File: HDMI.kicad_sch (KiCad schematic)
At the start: 8 parts, among them IC6 TPS2553QDBVRQ1, J9 HDMI_E

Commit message: small changes for ravi
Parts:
- removed C44: 100n, Capacitor_SMD:C_0402_1005Metric, symbol Device:C
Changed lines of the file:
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@@
-	)
-	(junction
-		(at 201.93 133.35)
-		(diameter 0)
-		(color 0 0 0 0)
 	)
 	(junction
@@
 	(wire
 		(pts
-			(xy 201.93 133.35) (xy 212.09 133.35)
-		)
-		(stroke
-			(width 0)
-			(type default)
-		)
-	)
-	(wire
-		(pts
 			(xy 146.05 120.65) (xy 152.4 120.65)
 		)
@@
 	(wire
 		(pts
-			(xy 185.42 133.35) (xy 201.93 133.35)
+			(xy 185.42 133.35) (xy 212.09 133.35)
 		)
 		(stroke
@@
 	(wire
 		(pts
-			(xy 201.93 146.05) (xy 201.93 149.86)
-		)
-		(stroke
-			(width 0)
-			(type default)
-		)
-	)
-	(wire
-		(pts
 			(xy 109.22 107.95) (xy 111.76 107.95)
 		)
@@
 		(pts
 			(xy 149.86 138.43) (xy 157.48 138.43)
-		)
-		(stroke
-			(width 0)
-			(type default)
-		)
-	)
-	(wire
-		(pts
-			(xy 201.93 133.35) (xy 201.93 138.43)
 		)
 		(stroke
@@
 			)
 		)
-		(property "Datasheet" ""
+		(property "Datasheet" "https://datasheets.raspberrypi.com/cm4/cm4-datasheet.pdf"
 			(at 81.28 127 0)
 			(effects
@@
 					(unit 1)
 				)
-			)
-		)
-	)
-	(symbol
-		(lib_id "Device:C")
-		(at 201.93 142.24 0)
-		(unit 1)
-		(exclude_from_sim no)
-		(in_bom yes)
-		(on_board yes)
-		(dnp no)
-		(property "Reference" "C44"
-			(at 204.851 141.0716 0)
-			(effects
-				(font
-					(size 1.27 1.27)
-				)
-				(justify left)
-			)
-		)
-		(property "Value" "100n"
-			(at 204.851 143.383 0)
-			(effects
-				(font
-					(size 1.27 1.27)
-				)
-				(justify left)
-			)
-		)
-		(property "Footprint" "Capacitor_SMD:C_0402_1005Metric"
-			(at 202.8952 146.05 0)
-			(effects
-				(font
-					(size 1.27 1.27)
-				)
-				(hide yes)
-			)
-		)
-		(property "Datasheet" "https://search.murata.co.jp/Ceramy/image/img/A01X/G101/ENG/GRM155R71C104KA88-01.pdf"
-			(at 201.93 142.24 0)
-			(effects
-				(font
-					(size 1.27 1.27)
-				)
-				(hide yes)
-			)
-		)
-		(property "Description" ""
-			(at 201.93 142.24 0)
-			(effects
-				(font
-					(size 1.27 1.27)
-				)
-				(hide yes)
-			)
-		)
-		(property "Field4" "Farnell"
-			(at 201.93 142.24 0)
-			(effects
-				(font
-					(size 1.27 1.27)
-				)
-				(hide yes)
-			)
-		)
-		(property "Field5" "2611911"
-			(at 201.93 142.24 0)
-			(effects
-				(font
-					(size 1.27 1.27)
-				)
-				(hide yes)
-			)
-		)
-		(property "Field6" "RM EMK105 B7104KV-F"
-			(at 201.93 142.24 0)
-			(effects
-				(font
-					(size 1.27 1.27)
-				)
-				(hide yes)
-			)
-		)
-		(property "Field7" "TAIYO YUDEN EUROPE GMBH"
-			(at 201.93 142.24 0)
-			(effects
-				(font
-					(size 1.27 1.27)
-				)
-				(hide yes)
-			)
-		)
-		(property "Part Description" "	0.1uF 10% 16V Ceramic Capacitor X7R 0402 (1005 Metric)"
-			(at 201.93 142.24 0)
-			(effects
-				(font
-					(size 1.27 1.27)
-				)
-				(hide yes)
-			)
-		)
-		(property "Field8" "110091611"
-			(at 201.93 142.24 0)
-			(effects
-				(font
-					(size 1.27 1.27)
-				)
-				(hide yes)
-			)
-		)
-		(pin "1"
-		)
-		(pin "2"
-		)
-		(instances
-			(project "PiBoard"
-				(path "/e4d65698-b8ec-4bf6-9f2b-a5010377155a/2dec5fd6-8756-425d-9ae9-2f1c2fc4e6c1"
-					(reference "C44")
-					(unit 1)
-				)
-			)
-		)
-	)
-	(symbol
-		(lib_name "GND_1")
-		(lib_id "power:GND")
-		(at 201.93 149.86 0)
-		(unit 1)
-		(exclude_from_sim no)
-		(in_bom yes)
-		(on_board yes)
-		(dnp no)
-		(fields_autoplaced yes)
-		(property "Reference" "#PWR063"
-			(at 201.93 156.21 0)
-			(effects
-				(font
-					(size 1.27 1.27)
-				)
-				(hide yes)
-			)
-		)
-		(property "Value" "GND"
-			(at 201.93 154.94 0)
-			(effects
-				(font
-					(size 1.27 1.27)
-				)
-				(hide yes)
-			)
-		)
-		(property "Footprint" ""
-			(at 201.93 149.86 0)
-			(effects
-				(font
-					(size 1.27 1.27)
-				)
-				(hide yes)
-			)
-		)
-		(property "Datasheet" ""
-			(at 201.93 149.86 0)
-			(effects
-				(font
-					(size 1.27 1.27)
-				)
-				(hide yes)
-			)
-		)
-		(property "Description" "Power symbol creates a global label with name \"GND\" , ground"
-			(at 201.93 149.86 0)
-			(effects
-				(font
-					(size 1.27 1.27)
-				)
-				(hide yes)
-			)
-		)
-		(pin "1"
-		)
-		(instances
-			(project "PiBoard"
-				(path "/e4d65698-b8ec-4bf6-9f2b-a5010377155a/2dec5fd6-8756-425d-9ae9-2f1c2fc4e6c1"
-					(reference "#PWR063")
-					(unit 1)
-				)

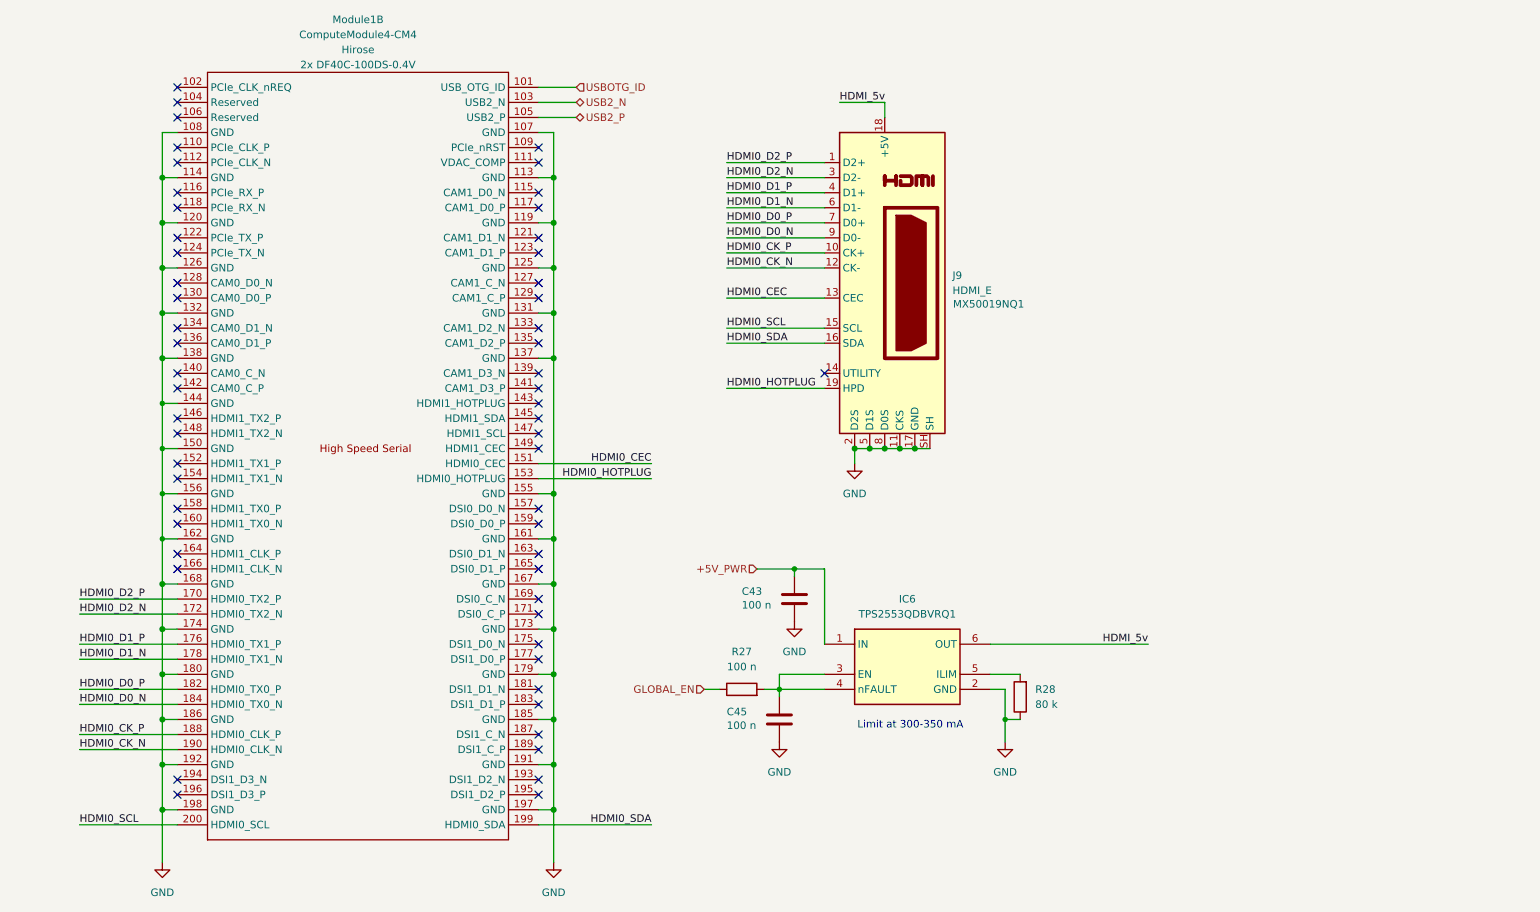
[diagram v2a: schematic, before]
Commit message: added parts to almost everything (except can xtal and fuses)
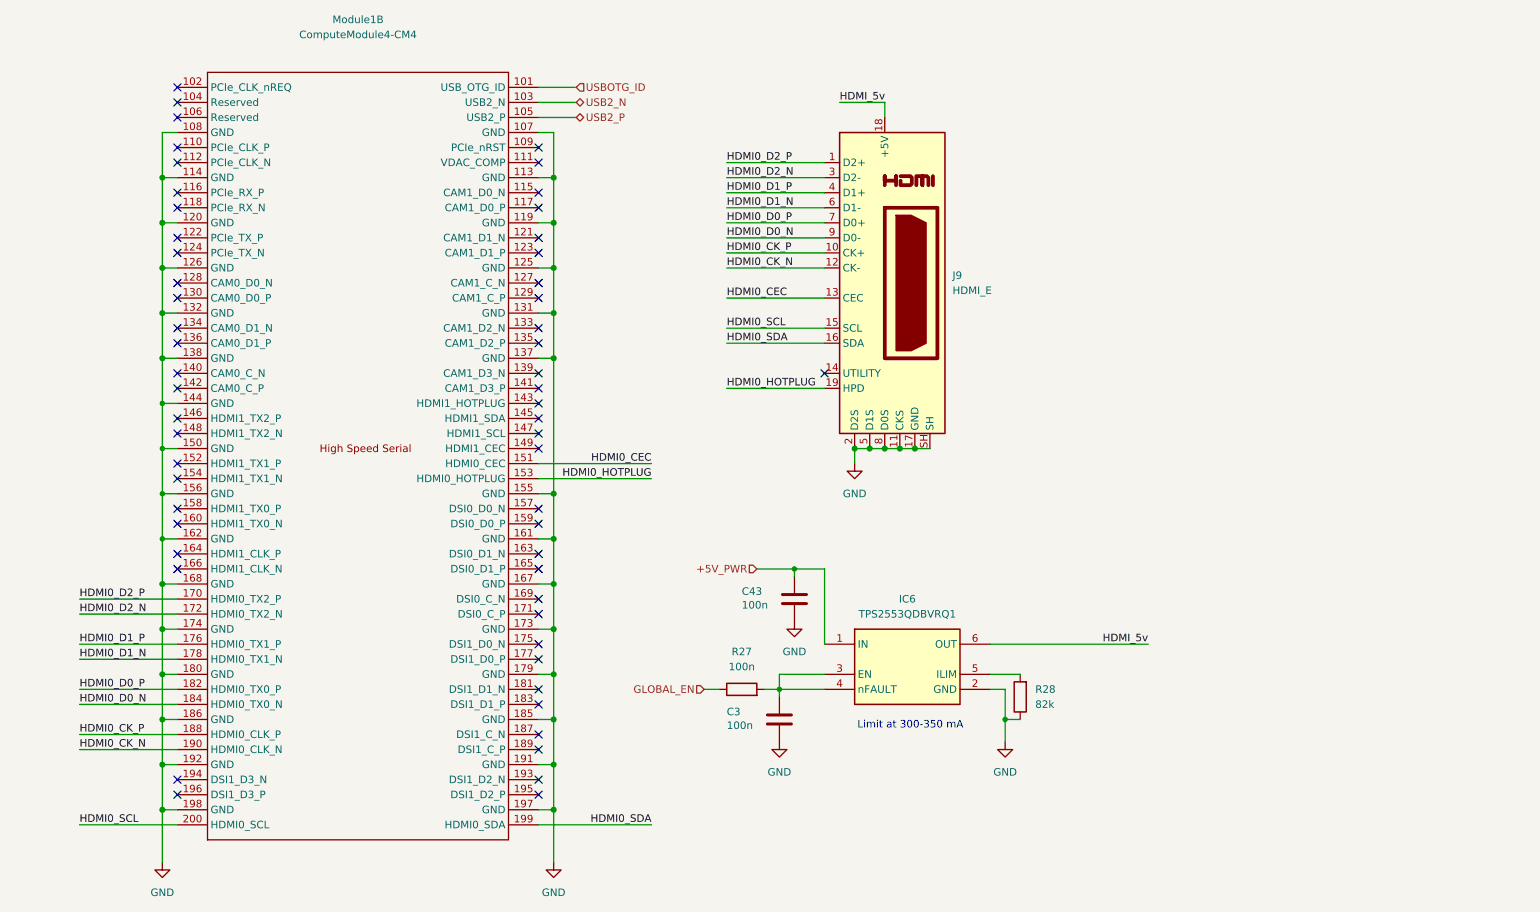
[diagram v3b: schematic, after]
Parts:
- removed C45: 100 n, Capacitor_SMD:C_0402_1005Metric, symbol Device:C
- added C3: 100n, Capacitor_SMD:C_0805_2012Metric, symbol Device:C
- C43: value 100 n -> 100n; footprint Capacitor_SMD:C_0402_1005Metric -> Capacitor_SMD:C_0805_2012Metric; Field4 Farnell -> (none); Field5 2611911 -> (none); Field6 RM EMK105 B7104KV-F -> (none); Field7 TAIYO YUDEN EUROPE GMBH -> (none); Field8 110091611 -> (none); P/N (none) -> C0805C104M5RACTU; Part Description 0.1uF 10% 16V Ceramic Capacitor X7R 0402 (1005 Metric) -> (none)
- IC6: footprint SOT95P280X145-6N -> Controls_Pi:SOT95P280X145-6N; Arrow Part Number TPS2553QDBVRQ1 -> (none); Arrow Price/Stock https://www.arrow.com/en/products/tps2553qdbvrq1/texas-inst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 -> (none); Height 1.45 -> (none); Manufacturer_Name Texas Instruments -> (none); Manufacturer_Part_Number TPS2553QDBVRQ1 -> (none); Mouser Part Number 595-TPS2553QDBVRQ1 -> (none); Mouser Price/Stock https://www.mouser.co.uk/ProductDetail/Texas-Instruments/TP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 -> (none); P/N (none) -> TPS2553QDBVRQ1
- J9: footprint (none) -> Controls_Pi:MX50019NQ1; Part No MX50019NQ1 -> (none)
- Module1: Field4 Hirose -> (none); Field5 2x DF40C-100DS-0.4V -> (none)
- R27: value 100 n -> 100n; footprint (none) -> Resistor_SMD:R_0805_2012Metric; P/N (none) -> CRCW0805100KFKEAC
- R28: value 80 k -> 82k; footprint (none) -> Resistor_SMD:R_1210_3225Metric; P/N (none) -> CRMA1210AF82K0FKEF
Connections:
- net GND: now also C3.2
- net at IC6.3 (EN), IC6.4 (nFAULT), R27.2: now also C3.1

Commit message: fixed cap sizes, added remaining parts, fixed rtc battery
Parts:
- J9: P/N (none) -> MX50019NQ1
- Module1: P/N (none) -> DF40C-100DS-0.4V
- R28: footprint Resistor_SMD:R_1210_3225Metric -> Resistor_SMD:R_0805_2012Metric; P/N CRMA1210AF82K0FKEF -> CRCW080582K0FKEAC
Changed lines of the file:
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@@
+			)
+		)
+		(property "P/N" "MX50019NQ1"
+			(at 167.64 72.39 0)
+			(effects
+				(font
+					(size 1.27 1.27)
+				)
+				(hide yes)
 			)
 		)
@@
 			)
 		)
-		(property "Footprint" "Resistor_SMD:R_1210_3225Metric"
+		(property "Footprint" "Resistor_SMD:R_0805_2012Metric"
 			(at 192.278 142.24 90)
 			(effects
@@
 			)
 		)
-		(property "Datasheet" "https://www.vishay.com/docs/68043/crma.pdf"
+		(property "Datasheet" "https://www.vishay.com/docs/28773/crcwce3.pdf"
 			(at 190.5 142.24 0)
 			(effects
@@
 			)
 		)
-		(property "Description" "Resistor 82k, 1%, 100PPM"
+		(property "Description" "Resistor 82k 1% 125mW"
 			(at 190.5 142.24 0)
 			(effects
@@
 			)
 		)
-		(property "P/N" "CRMA1210AF82K0FKEF"
+		(property "P/N" "CRCW080582K0FKEAC"
 			(at 190.5 142.24 0)
 			(effects
@@
 			)
 		)
-		(property "Description" ""
+		(property "Description" "100 Position Connector Receptacle, Center Strip Contacts Surface Mount Gold"
 			(at -60.96 100.33 0)
 			(effects
+				(font
+					(size 1.27 1.27)
+				)
+				(hide yes)
+			)
+		)
+		(property "P/N" "DF40C-100DS-0.4V"
+			(at -60.96 100.33 0)
+			(effects

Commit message: review committee changes implmented
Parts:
- added D10, D8: ESD204DQAR, Controls_Pi:ESD204DQAR, symbol ESD204DQAR:ESD204DQAR
- added D12: TPD4E05U06DQAR, DQA(R-PUSON-N10), symbol TPD4E05U06DQAR:TPD4E05U06DQAR
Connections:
- net GND: now also D10.3 (GND_1), D10.8 (GND_2), D8.3 (GND_1), D8.8 (GND_2)
- net HDMI0_CEC: now also D12.4 (D2+); no longer J9.13 (CEC)
- net HDMI0_CK_N: now also D10.5 (IO4); no longer J9.12 (CK-)
- net HDMI0_CK_P: now also D10.4 (IO3); no longer J9.10 (CK+)
- net HDMI0_D0_N: now also D8.2 (IO2); no longer J9.9 (D0-)
- net HDMI0_D0_P: now also D8.1 (IO1); no longer J9.7 (D0+)
- net HDMI0_D1_N: now also D8.5 (IO4); no longer J9.6 (D1-)
- net HDMI0_D1_P: now also D8.4 (IO3); no longer J9.4 (D1+)
- net HDMI0_D2_N: now also D10.2 (IO2); no longer J9.3 (D2-)
- net HDMI0_D2_P: now also D10.1 (IO1); no longer J9.1 (D2+)
- net HDMI0_SCL: now also D12.1 (D1+); no longer J9.15 (SCL)
- net HDMI0_SDA: now also D12.2 (D1-); no longer J9.16 (SDA)
- net HDMI_5v renamed HDMI_5V
- new net HDMI0_CEC_P: D12.7 (NC_2), J9.13 (CEC)
- new net HDMI0_CK_N_P: D10.7 (NC_2), J9.12 (CK-)
- new net HDMI0_CK_P_P: D10.6 (NC_1), J9.10 (CK+)
- new net HDMI0_D0_N_P: D8.10 (NC_4), J9.9 (D0-)
- new net HDMI0_D0_P_P: D8.9 (NC_3), J9.7 (D0+)
- new net HDMI0_D1_N_P: D8.7 (NC_2), J9.6 (D1-)
- new net HDMI0_D1_P_P: D8.6 (NC_1), J9.4 (D1+)
- new net HDMI0_D2_N_P: D10.10 (NC_4), J9.3 (D2-)
- new net HDMI0_D2_P_P: D10.9 (NC_3), J9.1 (D2+)
- new net HDMI0_SCL_P: D12.10 (NC_4), J9.15 (SCL)
- new net HDMI0_SDA_P: D12.9 (NC_3), J9.16 (SDA)
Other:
- note added: "ESD Protection Diodes for HDMI"
- moved on the sheet: C3, C43, IC6, J9, Module1B, R27, R28

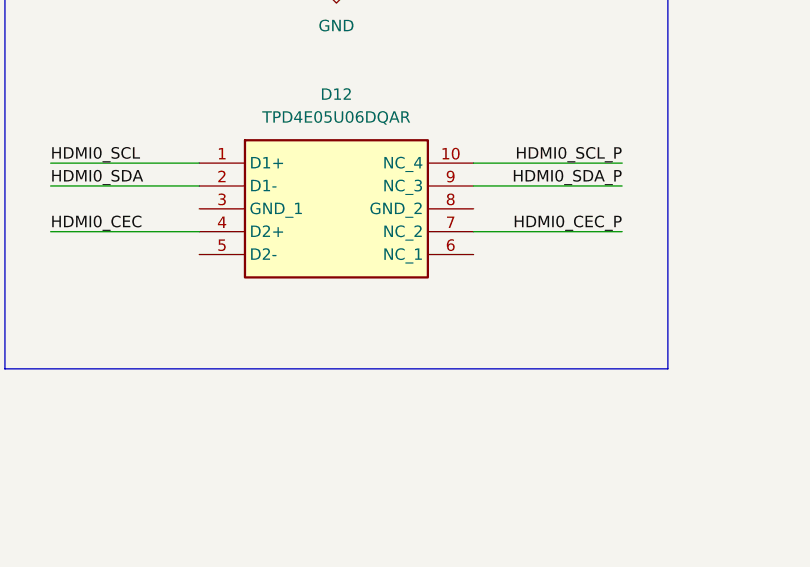
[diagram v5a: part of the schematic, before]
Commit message: fixed relevant erc errors
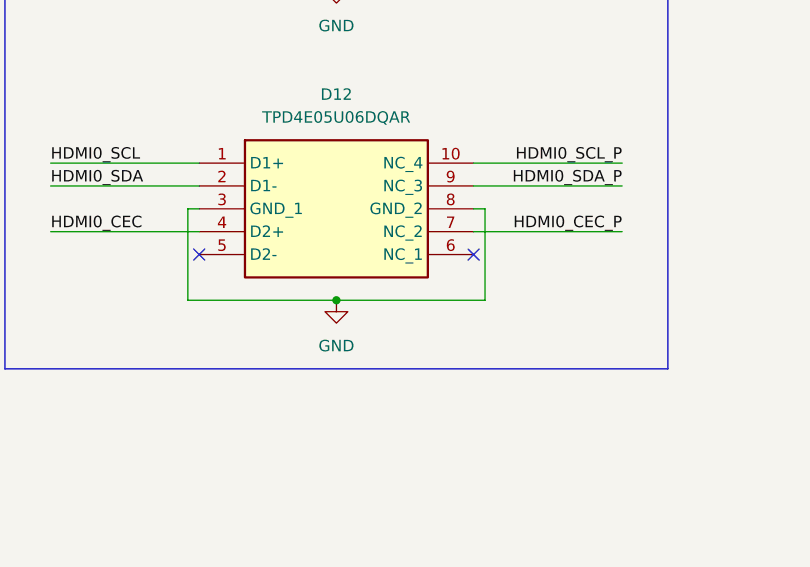
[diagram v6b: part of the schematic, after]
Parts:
- D12: footprint DQA(R-PUSON-N10) -> Controls_Pi:DQA_R-PUSON-N10_
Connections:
- net GND: now also D12.3 (GND_1), D12.8 (GND_2)
- no-connect marks 56 -> 58
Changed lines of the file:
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@@
 	)
 	(junction
+		(at 157.48 144.78)
+		(diameter 0)
+		(color 0 0 0 0)
+	)
+	(junction
 		(at 34.29 146.05)
 		(diameter 1.016)
@@
 	)
 	(no_connect
+		(at 142.24 139.7)
+	)
+	(no_connect
 		(at 97.79 92.71)
 	)
@@
 	)
 	(no_connect
+		(at 172.72 139.7)
+	)
+	(no_connect
 		(at 97.79 82.55)
 	)
@@
 	(wire
 		(pts
+			(xy 142.24 134.62) (xy 140.97 134.62)
+		)
+		(stroke
+			(width 0)
+			(type default)
+		)
+	)
+	(wire
+		(pts
 			(xy 246.38 149.86) (xy 248.92 149.86)
 		)
@@
 	(wire
 		(pts
+			(xy 140.97 134.62) (xy 140.97 144.78)
+		)
+		(stroke
+			(width 0)
+			(type default)
+		)
+	)
+	(wire
+		(pts
 			(xy 97.79 105.41) (xy 116.84 105.41)
 		)
@@
 	(wire
 		(pts
+			(xy 140.97 144.78) (xy 157.48 144.78)
+		)
+		(stroke
+			(width 0)
+			(type default)
+		)
+	)
+	(wire
+		(pts
 			(xy 241.3 149.86) (xy 243.84 149.86)
 		)
@@
 	(wire
 		(pts
+			(xy 173.99 134.62) (xy 173.99 144.78)
+		)
+		(stroke
+			(width 0)
+			(type default)
+		)
+	)
+	(wire
+		(pts
 			(xy 172.72 60.96) (xy 189.23 60.96)
 		)
@@
 	(wire
 		(pts
-			(xy 189.23 137.16) (xy 172.72 137.16)
+			(xy 172.72 137.16) (xy 189.23 137.16)
 		)
 		(stroke
@@
 	(wire
 		(pts
+			(xy 172.72 134.62) (xy 173.99 134.62)
+		)
+		(stroke
+			(width 0)
+			(type default)
+		)
+	)
+	(wire
+		(pts
 			(xy 100.33 161.29) (xy 100.33 170.18)
 		)
@@
 	(wire
 		(pts
+			(xy 173.99 144.78) (xy 157.48 144.78)
+		)
+		(stroke
+			(width 0)
+			(type default)
+		)
+	)
+	(wire
+		(pts
 			(xy 219.71 129.54) (xy 236.22 129.54)
 		)
@@
 			)
 		)
-		(property "Footprint" "DQA(R-PUSON-N10)"
+		(property "Footprint" "Controls_Pi:DQA_R-PUSON-N10_"
 			(at 168.91 224.46 0)
 			(effects
@@
 					(unit 1)
 				)
+			)
+		)
+	)
+	(symbol
+		(lib_id "power:GND")
+		(at 157.48 144.78 0)
+		(unit 1)
+		(exclude_from_sim no)
+		(in_bom yes)
+		(on_board yes)
+		(dnp no)
+		(fields_autoplaced yes)
+		(property "Reference" "#PWR095"
+			(at 157.48 151.13 0)
+			(effects
+				(font
+					(size 1.27 1.27)
+				)
+				(hide yes)
+			)
+		)
+		(property "Value" "GND"
+			(at 157.48 149.86 0)
+			(effects
+				(font
+					(size 1.27 1.27)
+				)
+			)
+		)
+		(property "Footprint" ""
+			(at 157.48 144.78 0)
+			(effects
+				(font
+					(size 1.27 1.27)
+				)
+				(hide yes)
+			)
+		)
+		(property "Datasheet" ""
+			(at 157.48 144.78 0)
+			(effects
+				(font
+					(size 1.27 1.27)
+				)
+				(hide yes)
+			)
+		)
+		(property "Description" "Power symbol creates a global label with name \"GND\" , ground"
+			(at 157.48 144.78 0)
+			(effects
+				(font
+					(size 1.27 1.27)
+				)
+				(hide yes)
+			)
+		)
+		(pin "1"
+		)
+		(instances
+			(project "PiBoard"
+				(path "/e4d65698-b8ec-4bf6-9f2b-a5010377155a/2dec5fd6-8756-425d-9ae9-2f1c2fc4e6c1"
+					(reference "#PWR095")
+					(unit 1)
+				)

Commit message: layout 1.0 kinda done
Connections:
- net HDMI0_CEC: now also D12.1 (D1+); no longer D12.4 (D2+)
- net HDMI0_CK_N: now also D10.1 (IO1); no longer D10.5 (IO4)
- net HDMI0_CK_P: now also D10.2 (IO2); no longer D10.4 (IO3)
- net HDMI0_D0_N: now also D8.5 (IO4); no longer D8.2 (IO2)
- net HDMI0_D0_P: now also D8.4 (IO3); no longer D8.1 (IO1)
- net HDMI0_D1_N: now also D10.4 (IO3); no longer D8.5 (IO4)
- net HDMI0_D1_P: now also D10.5 (IO4); no longer D8.4 (IO3)
- net HDMI0_D2_N: now also D8.2 (IO2); no longer D10.2 (IO2)
- net HDMI0_D2_P: now also D8.1 (IO1); no longer D10.1 (IO1)
- net HDMI0_SCL: now also D12.4 (D2+); no longer D12.1 (D1+)
- net HDMI0_SDA: now also D12.5 (D2-); no longer D12.2 (D1-)
- net HDMI0_SCL_PRT: now reaches D12.6 (NC_1)
- net HDMI0_SCL_PRT: now also J9.15 (SCL)
- net HDMI0_CEC_P renamed HDMI0_CEC_PRT
- net HDMI0_CEC_PRT: now also D12.10 (NC_4); no longer D12.7 (NC_2)
- net HDMI0_CK_N_P renamed HDMI0_CK_PRT_N
- net HDMI0_CK_PRT_N: now also D10.10 (NC_4); no longer D10.7 (NC_2)
- net HDMI0_CK_P_P renamed HDMI0_CK_PRT_P
- net HDMI0_CK_PRT_P: now also D10.9 (NC_3); no longer D10.6 (NC_1)
- net HDMI0_D0_N_P renamed HDMI0_D0_PRT_N
- net HDMI0_D0_PRT_N: now also D8.6 (NC_1); no longer D8.10 (NC_4)
- net HDMI0_D0_P_P renamed HDMI0_D0_PRT_P
- net HDMI0_D0_PRT_P: now also D8.7 (NC_2); no longer D8.9 (NC_3)
- net HDMI0_D1_N_P renamed HDMI0_D1_PRT_N
- net HDMI0_D1_PRT_N: now also D10.7 (NC_2); no longer D8.7 (NC_2)
- net HDMI0_D1_P_P renamed HDMI0_D1_PRT_P
- net HDMI0_D1_PRT_P: now also D10.6 (NC_1); no longer D8.6 (NC_1)
- net HDMI0_D2_N_P renamed HDMI0_D2_PRT_N
- net HDMI0_D2_PRT_N: now also D8.9 (NC_3); no longer D10.10 (NC_4)
- net HDMI0_D2_P_P renamed HDMI0_D2_PRT_P
- net HDMI0_D2_PRT_P: now also D8.10 (NC_4); no longer D10.9 (NC_3)
- removed net HDMI0_SCL_P: D12.10 (NC_4), J9.15 (SCL)
- net HDMI0_SDA_P: no longer names the net of D12.9 (NC_3)
- net HDMI0_SDA_P: no longer J9.16 (SDA)
- new net HDMI0_SDA_PRT: D12.7 (NC_2), J9.16 (SDA)
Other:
- note added: "HELPPPP! CAN I DO N, P, instead of P, N order?????"
- note added: "Pinout for ESD diodes configured for easy layout"

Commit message: small notes
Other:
- note added: "I think it should be ok, as long as they are in N/P pairs - Mika"
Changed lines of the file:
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@@
+		)
+	)
+	(text "I think it should be ok, as long\nas they are in N/P pairs\n- Mika\n"
+		(exclude_from_sim no)
+		(at 213.868 98.806 0)
+		(effects
+			(font
+				(size 1.27 1.27)
+			)
 		)
 	)
